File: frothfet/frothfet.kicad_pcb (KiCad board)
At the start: 4 copper layers, 144 x 127 mm, 283 parts, among them J1 Conn_01x06, J10 Conn_01x01_Pin, J11 Screw_Terminal_01x08, J12 Screw_Terminal_01x08, J13 USB_TYPE_C_16PIN, J14 Conn_01x04, J2 Conn_01x06, J3 Conn_01x04_MountingPin, J4 Conn_01x01_Pin, J5 Conn_01x01_Pin, J6 Conn_01x01_Pin, J7 Conn_01x01_Pin, J8 Conn_01x01_Pin, J9 Conn_01x01_Pin, M1 Fan_Tacho, M2 Fan_Tacho, Q1 BSC010N04LS, Q10 AO3400A, Q11 AO3400A, Q2 BSC010N04LS, Q3 BSC010N04LS, Q4 BSC010N04LS, Q5 BSC010N04LS, Q6 BSC010N04LS, Q7 BSC010N04LS, Q8 BSC010N04LS, Q9 AO3400A, SW1 BOOT, SW2 RESET, U1 74AHC541, U10 LM75BD, U11 LM74502H, U12 INA226, U13 LM75BD, U14 LM74502H, U15 INA226, U16 LM75BD, U17 LM74502H, U18 INA226, U19 LM75BD, U2 LM74502H, U20 LM74502H, U21 INA226, U22 LM75BD, U23 LM74502H, U24 INA226, U25 LM75BD, U26 TPS7A2033PDBVR, U27 XL1509-5.0, U28 MCP3425A0T-ECH, U29 MAX40200AUK, U3 INA226, U30 ESP32-S3-WROOM-1-N16R8, U31 USBLC6-2SC6, U32 SN74LV1T34DBV, U33 XC6210B332MR, U4 LM75BD, U5 LM74502H, U6 INA226, U7 LM75BD, U8 LM74502H, U9 INA226

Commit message: fully routed
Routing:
- net Net-(D27-A): track 19.4 -> 96.5 mm, vias 0 -> 1
- net FAN_TACH1: track 0.00 -> 63.8 mm, vias 0 -> 2
- net FAN_TACH2: track 0.00 -> 56.7 mm, vias 0 -> 2
- net FAN_MOSFET1: track 0.00 -> 54.9 mm, vias 0 -> 2
- net CHANNEL_LEDS: track 1.26 -> 54.9 mm, vias 1 -> 2
- net FAN_MOSFET2: track 0.00 -> 49.2 mm, vias 0 -> 2
- net PIEZO: track 0.00 -> 48.1 mm, vias 0 -> 2
- net /ESP32-S3/GPIO0_BOOT: track 7.34 -> 48.8 mm, vias 0 -> 1
- net /ESP32-S3/GPIO4: track 0.00 -> 39.6 mm, vias 0 -> 2
- net /ESP32-S3/GPIO5: track 0.00 -> 38.1 mm, vias 0 -> 2
- net /ESP32-S3/GPIO6: track 0.00 -> 36.9 mm, vias 0 -> 2
- net /ESP32-S3/ESP_RXD0: track 0.00 -> 35.2 mm, vias 0 -> 2
- net /ESP32-S3/GPIO7: track 0.00 -> 35.0 mm, vias 0 -> 2
- net /ESP32-S3/EN: track 7.34 -> 41.3 mm, vias 0 -> 1
- net /ESP32-S3/ESP_TXD0: track 0.00 -> 32.4 mm, vias 0 -> 2
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
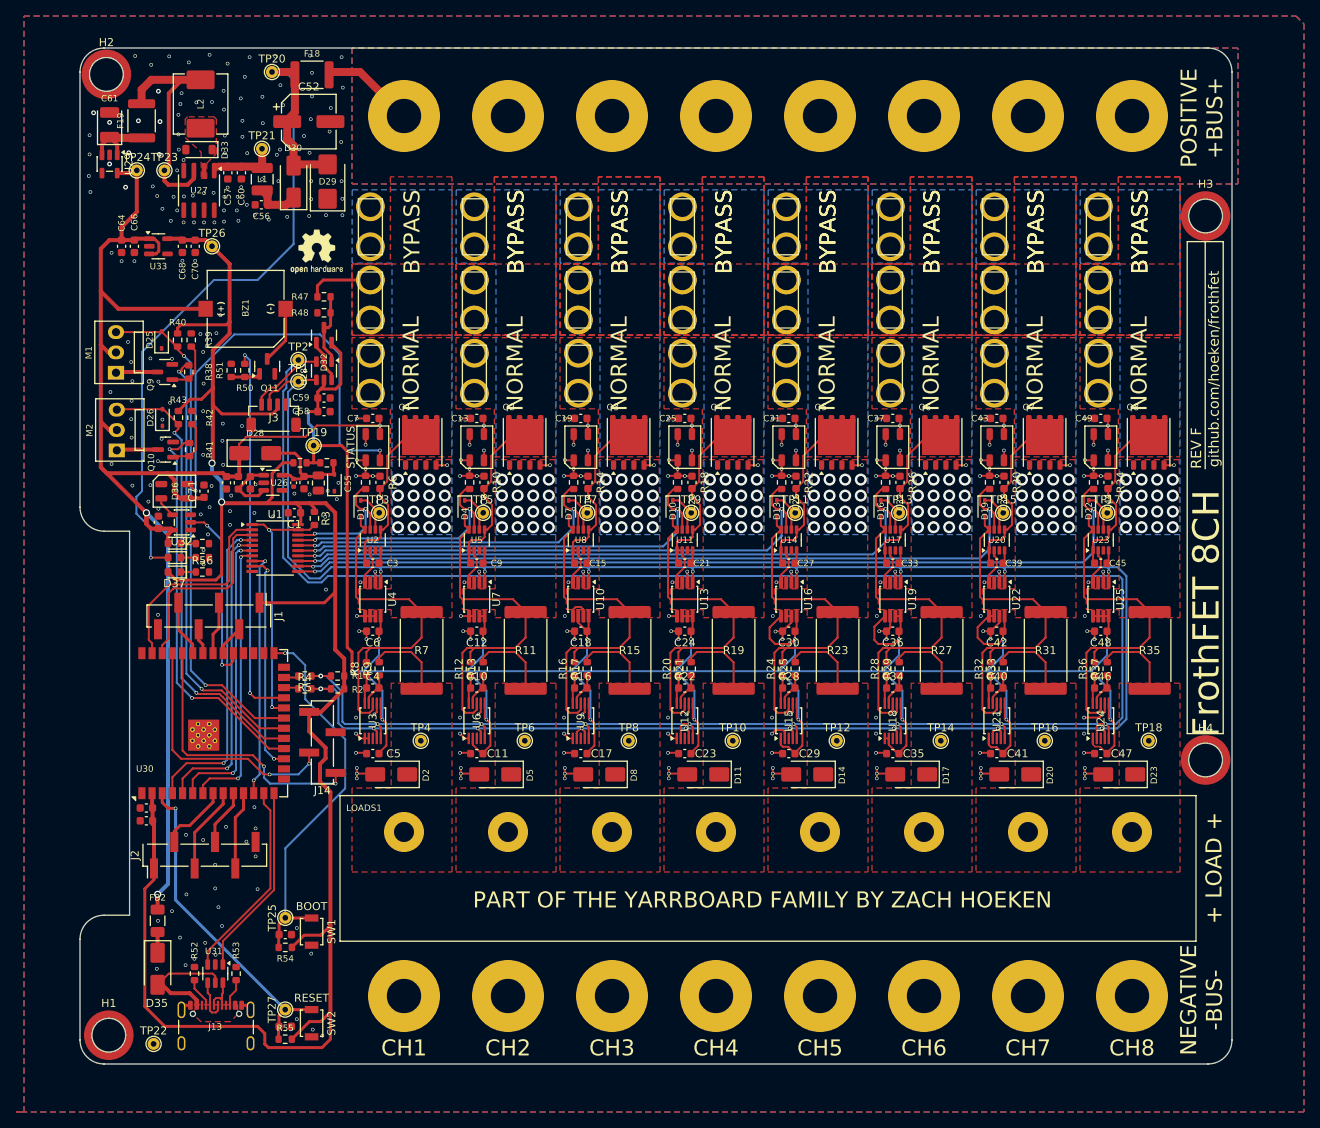
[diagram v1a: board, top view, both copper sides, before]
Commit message: added via stitching
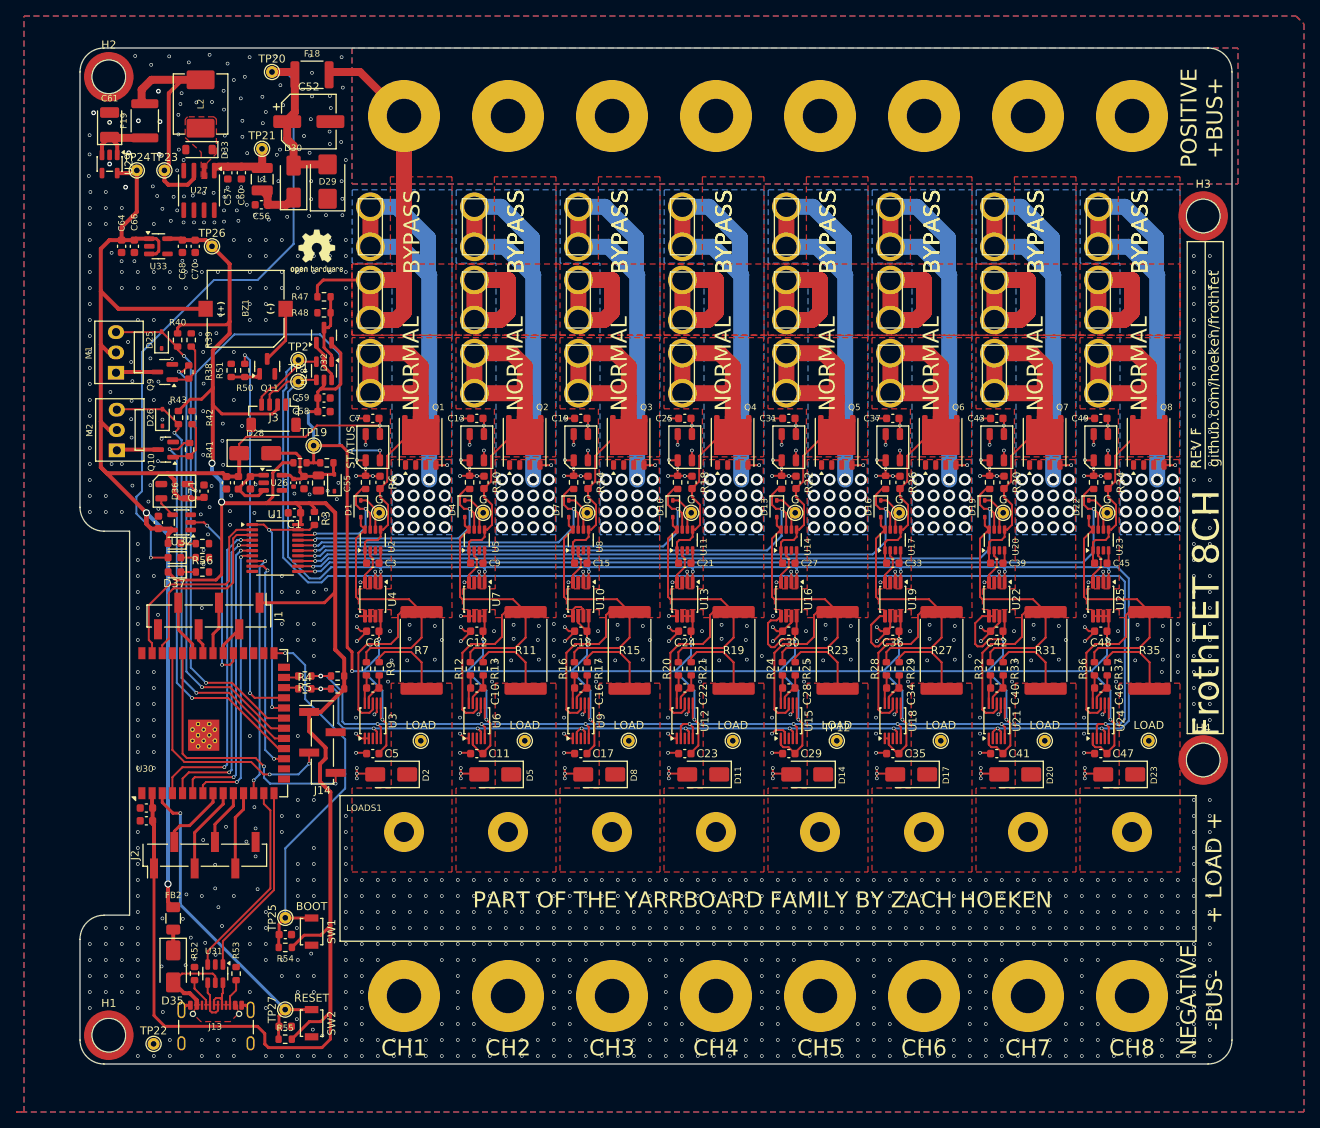
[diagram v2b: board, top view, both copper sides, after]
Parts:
- moved D35 1.97 mm to (64.7, 142.8)
- moved FB2 1.97 mm to (64.7, 136.8)
- moved H2 0.42 mm to (56.6, 31.6)
- moved F19 0.40 mm to (61.1, 37.1)
- moved H3 0.30 mm to (193.4, 49.0)
- moved H4 0.30 mm to (193.4, 117.0)
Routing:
- net +24V: track 20.1 -> 183.1 mm
- net /CHANNEL 3/LOAD_SWITCHED: track 43.5 -> 106.3 mm
- net /CHANNEL 2/LOAD_SWITCHED: track 43.5 -> 106.3 mm
- net /CHANNEL 1/LOAD_SWITCHED: track 43.5 -> 106.3 mm
- net /CHANNEL 6/LOAD_SWITCHED: track 43.5 -> 106.3 mm
- net /CHANNEL 8/LOAD_SWITCHED: track 43.5 -> 106.3 mm
- net /CHANNEL 7/LOAD_SWITCHED: track 43.5 -> 106.3 mm
- net /CHANNEL 5/LOAD_SWITCHED: track 43.5 -> 106.3 mm
- net /CHANNEL 4/LOAD_SWITCHED: track 43.5 -> 106.3 mm
- net /CHANNEL 1/LOAD_VSS: track 21.6 -> 49.0 mm
- net /CHANNEL 2/LOAD_VSS: track 21.6 -> 49.0 mm
- net /CHANNEL 3/LOAD_VSS: track 21.6 -> 49.0 mm
- net /CHANNEL 7/LOAD_VSS: track 21.6 -> 49.0 mm
- net /CHANNEL 6/LOAD_VSS: track 21.6 -> 49.0 mm
- net /CHANNEL 5/LOAD_VSS: track 21.6 -> 49.0 mm
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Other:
- board text added: "G"
- board text added: "LOAD"

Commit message: drc errors fixed.
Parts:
- U10, U13, U16, U19, U22, U25, U4, U7: footprint Package_SO:VSSOP-8_3x3mm_P0.65mm -> Package_SO:MSOP-8_3x3mm_P0.65mm
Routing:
- net GND: track 212.5 -> 209.6 mm, vias 1130 -> 1129
- net +3.3VADC: track 368.4 -> 365.6 mm
- net +5V: track 290.0 -> 287.7 mm
- net /CHANNEL 3/LOAD_VSS: track 49.0 -> 46.9 mm
- net /CHANNEL 7/LOAD_VSS: track 49.0 -> 46.9 mm
- net /CHANNEL 6/LOAD_VSS: track 49.0 -> 46.9 mm
- net /CHANNEL 4/LOAD_VSS: track 49.0 -> 46.9 mm
- net /CHANNEL 2/LOAD_VSS: track 49.0 -> 46.9 mm
- net /CHANNEL 1/LOAD_VSS: track 49.0 -> 46.9 mm
- net /CHANNEL 5/LOAD_VSS: track 49.0 -> 46.9 mm
- net /CHANNEL 8/LOAD_VSS: track 49.0 -> 46.9 mm
- net SDA: track 293.9 -> 292.5 mm
- net /CHANNEL 8/LED_DOUT: track 1.34 -> 0.00 mm, vias 1 -> 0
- net PWM3: track 45.8 -> 44.7 mm
- net SCL: track 304.3 -> 303.3 mm
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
